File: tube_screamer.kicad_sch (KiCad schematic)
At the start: 68 parts, among them J1 Jack_6.35, J2 Jack_6.35, J3 Conn_01x05, J4 Conn_01x05, J5 Conn_01x05, J6 Barrel_Jack_Switch, J7 Conn_01x01_Socket, J8 Conn_01x01_Socket, P1 tube_screamer_front_panel, Q1 MMBT5551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

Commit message: Production files v1.
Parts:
- BT1, C2, C8, D8, D9, J1, J2, J3, J4, J5, J6, P1, RV5, RV6, RV8, SW1: now not fitted
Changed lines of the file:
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@@
 		(in_bom yes)
 		(on_board yes)
-		(dnp no)
+		(dnp yes)
 		(fields_autoplaced yes)
 		(property "Reference" "J3"
@@
 		(in_bom yes)
 		(on_board yes)
-		(dnp no)
+		(dnp yes)
 		(fields_autoplaced yes)
 		(property "Reference" "J6"
@@
 		(in_bom yes)
 		(on_board yes)
-		(dnp no)
+		(dnp yes)
 		(fields_autoplaced yes)
 		(property "Reference" "SW1"
@@
 		(in_bom yes)
 		(on_board yes)
-		(dnp no)
+		(dnp yes)
 		(property "Reference" "RV8"
 			(at 125.222 24.638 0)
@@
 		(in_bom yes)
 		(on_board yes)
-		(dnp no)
+		(dnp yes)
 		(fields_autoplaced yes)
 		(property "Reference" "D9"
@@
 		(in_bom yes)
 		(on_board yes)
-		(dnp no)
+		(dnp yes)
 		(fields_autoplaced yes)
 		(property "Reference" "SW1"
@@
 		(in_bom yes)
 		(on_board yes)
-		(dnp no)
+		(dnp yes)
 		(fields_autoplaced yes)
 		(property "Reference" "D8"
@@
 		(in_bom yes)
 		(on_board yes)
-		(dnp no)
+		(dnp yes)
 		(fields_autoplaced yes)
 		(property "Reference" "RV5"
@@
 		(in_bom yes)
 		(on_board yes)
-		(dnp no)
+		(dnp yes)
 		(property "Reference" "C8"
 			(at 81.28 178.4349 0)
@@
 		(in_bom yes)
 		(on_board yes)
-		(dnp no)
+		(dnp yes)
 		(fields_autoplaced yes)
 		(property "Reference" "J4"
@@
 		(in_bom yes)
 		(on_board yes)
-		(dnp no)
+		(dnp yes)
 		(fields_autoplaced yes)
 		(property "Reference" "P1"
@@
 		(in_bom yes)
 		(on_board yes)
-		(dnp no)
+		(dnp yes)
 		(fields_autoplaced yes)
 		(property "Reference" "C2"
@@
 		(in_bom yes)
 		(on_board yes)
-		(dnp no)
+		(dnp yes)
 		(property "Reference" "J1"
 			(at 24.13 52.0701 0)
@@
 		(in_bom yes)
 		(on_board yes)
-		(dnp no)
+		(dnp yes)
 		(property "Reference" "BT1"
 			(at 55.118 178.562 0)
@@
 		(in_bom yes)
 		(on_board yes)
-		(dnp no)
+		(dnp yes)
 		(property "Reference" "J2"
 			(at 270.51 127.0001 0)
@@
 		(in_bom yes)
 		(on_board yes)
-		(dnp no)
+		(dnp yes)
 		(property "Reference" "RV6"
 			(at 188.722 19.812 0)
@@
 		(in_bom yes)
 		(on_board yes)
-		(dnp no)
+		(dnp yes)
 		(property "Reference" "J5"
 			(at 119.38 110.49 0)

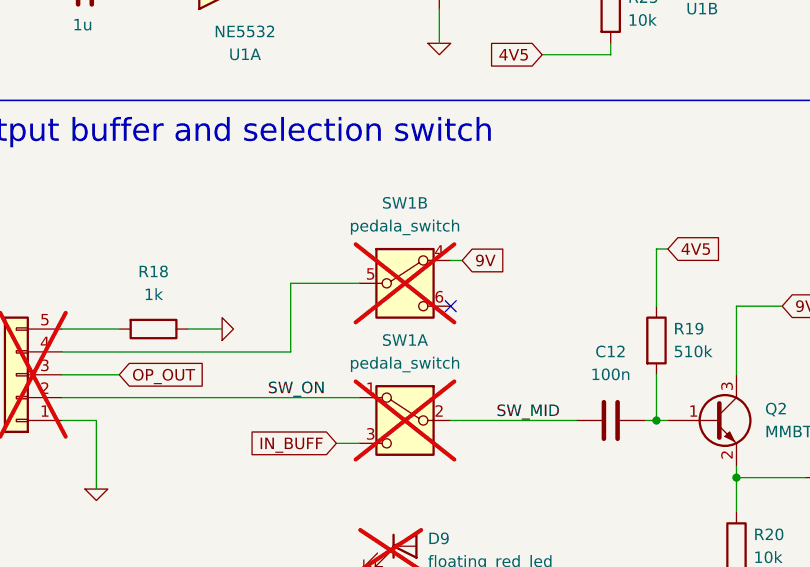
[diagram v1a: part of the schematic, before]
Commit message: Rotirani pinovi audio konektora, rotirani LED prekidač pinovi.
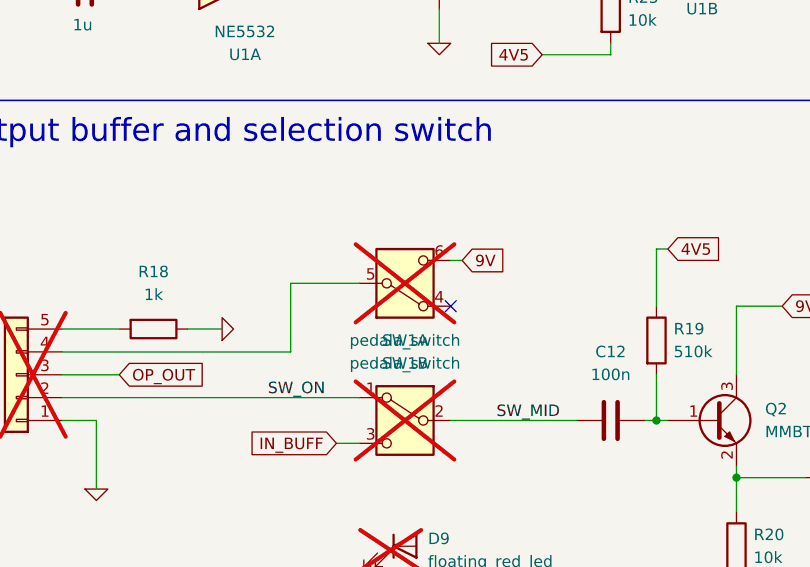
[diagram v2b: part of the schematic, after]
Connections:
- net 9V: now also SW1.6 (C); no longer SW1.4 (A)
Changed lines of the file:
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@@
 		(lib_id "pedale:pedala_switch")
 		(at 168.91 100.33 0)
+		(mirror x)
 		(unit 2)
 		(exclude_from_sim no)
@@
 		(on_board yes)
 		(dnp yes)
-		(fields_autoplaced yes)
 		(property "Reference" "SW1"
-			(at 168.91 91.44 0)
+			(at 168.91 109.22 0)
 			(effects
 				(font
@@
 		)
 		(property "Value" "pedala_switch"
-			(at 168.91 93.98 0)
+			(at 168.91 106.68 0)
 			(effects
 				(font
